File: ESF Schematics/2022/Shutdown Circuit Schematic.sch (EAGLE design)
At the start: 59 parts, among them K1 RELAY_DPDT_RT424009, K2 RELAY_SPST_NO_

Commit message: final drafts of most schematics
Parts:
- removed U$16: CONNECTOR-2_HPK, HyTechSymbolsTemp:CONNECTOR-2_HPK
- added J1, J2: CONNECTOR-1_LCAX2-14F-E, HyTechSymbolsTemp:CONNECTOR-1_LCAX2-14F-E
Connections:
- net TS+UNFUSED: now also J2.1; no longer U$16.1
- net TS-UNFUSED: now also J1.1; no longer U$16.2
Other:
- note added: "16AWG"
- note added: "16AWG:"
- note added: "17.5mm^2"
- note added: "17.5mm^2:"
- note added: "22AWG"
- note added: "22AWG:"
- note added: "Wire Gauge Key"
- moved on the sheet: F6

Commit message: ESF review changes
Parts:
- renumbered K1 to BSPD_RELAY
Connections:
- new net N$42: BSPD_RELAY.5, SOFTWARE_SHDN_RELAY.6
- net N$10: now also BSPD_RELAY.6
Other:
- note added: "HVD connectors Move interlocks outside put actual battery symbol Fix power switching circuit relay and add to datasheet Make TSMS after interlocks also reference accumulator notes ring terminals"
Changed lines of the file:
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@@
 <part name="P3" library="HyTechSupplies" deviceset="GND" device=""/>
 <part name="LATCHING" library="HyTechSymbolsTemp" deviceset="BUTTON_NO" device=""/>
-<part name="K1" library="HyTechSymbolsTemp" deviceset="RELAY_DPDT_?*" device="" technology="RT424009"/>
+<part name="BSPD_RELAY" library="HyTechSymbolsTemp" deviceset="RELAY_DPDT_?*" device="" technology="RT424009"/>
 <part name="U$7" library="HyTechSymbolsTemp" deviceset="DIODE" device=""/>
 <part name="U$8" library="HyTechSymbolsTemp" deviceset="DIODE" device=""/>
@@
 <text x="114.3" y="63.5" size="1.27" layer="97" align="top-left">22AWG</text>
 <text x="76.2" y="162.56" size="1.27" layer="97" align="top-left">22AWG</text>
+<text x="289.56" y="203.2" size="1.778" layer="88">HVD connectors
+Move interlocks outside
+put actual battery symbol
+Fix power switching circuit relay and add to datasheet
+Make TSMS after interlocks
+also reference accumulator notes
+ring terminals
+</text>
 </plain>
 <instances>
@@
 <attribute name="NAME" x="157.48" y="203.962" size="1.27" layer="95" align="bottom-center"/>
 </instance>
-<instance part="K1" gate="G$1" x="203.2" y="175.26" smashed="yes">
+<instance part="BSPD_RELAY" gate="G$1" x="203.2" y="175.26" smashed="yes">
 <attribute name="MPN" x="203.2" y="141.478" size="1.27" layer="96" align="top-left"/>
 <attribute name="NAME" x="203.2" y="176.022" size="1.27" layer="95"/>
@@
 <pinref part="AMS_RELAY" gate="G$1" pin="5"/>
 <wire x1="175.26" y1="149.86" x2="175.26" y2="147.32" width="0.1524" layer="91"/>
+<pinref part="BSPD_RELAY" gate="G$1" pin="6"/>
+<wire x1="175.26" y1="147.32" x2="200.66" y2="147.32" width="0.1524" layer="91"/>
 </segment>
 </net>
@@
 <pinref part="U$7" gate="G$1" pin="A"/>
 <wire x1="200.66" y1="167.64" x2="198.12" y2="167.64" width="0.1524" layer="91"/>
-<pinref part="K1" gate="G$1" pin="COIL-"/>
-<pinref part="K1" gate="G$1" pin="3"/>
+<pinref part="BSPD_RELAY" gate="G$1" pin="COIL-"/>
+<pinref part="BSPD_RELAY" gate="G$1" pin="3"/>
 <wire x1="200.66" y1="167.64" x2="200.66" y2="157.48" width="0.1524" layer="91"/>
 <junction x="200.66" y="167.64"/>
@@
 <pinref part="U$8" gate="G$1" pin="C"/>
 <wire x1="210.82" y1="182.88" x2="215.9" y2="182.88" width="0.1524" layer="91"/>
-<pinref part="K1" gate="G$1" pin="COIL+"/>
+<pinref part="BSPD_RELAY" gate="G$1" pin="COIL+"/>
 <wire x1="215.9" y1="167.64" x2="218.44" y2="167.64" width="0.1524" layer="91"/>
 <junction x="215.9" y="167.64"/>
@@
 </segment>
 </net>
+<net name="N$42" class="0">
+<segment>
+<pinref part="BSPD_RELAY" gate="G$1" pin="5"/>
+<wire x1="215.9" y1="149.86" x2="215.9" y2="147.32" width="0.1524" layer="91"/>
+<pinref part="SOFTWARE_SHDN_RELAY" gate="G$1" pin="6"/>
+<wire x1="215.9" y1="147.32" x2="241.3" y2="147.32" width="0.1524" layer="91"/>
+</segment>
+</net>

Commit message: fixups after the ESF review
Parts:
- removed K2: RELAY_SPST_NO_, HyTechSymbolsTemp:RELAY_SPST_NO_
- added GLV_BATTERY: BATTERY, HyTechSymbols:BATTERY
- added J3, J4: CONNECTOR-1_LCAX2-14F-E, HyTechSymbolsTemp:CONNECTOR-1_LCAX2-14F-E
- added K1: RELAY_SPST_NO_CMX60D20, HyTechSymbolsTemp:RELAY_SPST_NO_CMX60D20
- added U$20, U$34, U$35, U$36, U$37: MAINTENANCE_PLUG_104742-2, HyTechSymbolsTemp:MAINTENANCE_PLUG_104742-2
- added U$38, U$39, U$40: RING_TERMINAL_19054-0042, HyTechSymbolsTemp:RING_TERMINAL_19054-0042
- U$21, U$22, U$23, U$24, U$25: value CONNECTOR-2_104742-2 -> MAINTENANCE_PLUG_104742-2; device HyTechSymbolsTemp:CONNECTOR-2_104742-2 -> HyTechSymbolsTemp:MAINTENANCE_PLUG_104742-2
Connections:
- removed net VBAT: F1.1
- new net N$43: U$20.P$1, U$21.P$1
- new net N$44: U$22.P$1, U$23.P$1
- new net N$45: U$24.P$1, U$25.P$1
- new net N$46: U$36.P$1, U$37.P$1
- new net N$47: AIR-.CONTACT1, U$37.1
- new net N$48: F6.2, U$38.P$1
- new net N$50: F5.2, U$39.P$1
- new net N$51: HPK_INTERLOCK.S, TSMS.P
- net GND: now also GLV_BATTERY.P$2, K1.COIL+; no longer K2.COIL+
- net N$13: now also HVD_INTERLOCK.P; no longer TSMS.P
- net N$14: now also F1.1, GLV_BATTERY.P$1; no longer HVD_INTERLOCK.P, TSMS.S
- net N$15: now also K1.CONTACT1; no longer K2.CONTACT1
- net N$16: now also K1.CONTACT2; no longer K2.CONTACT2
- net N$17: now also K1.COIL-; no longer K2.COIL-
- net N$23: now also U$36.1; no longer U$24.2
- net N$31: now also U$20.1; no longer U$21.2
- net N$33: now also U$22.1; no longer U$22.2
- net N$34: now also U$23.1; no longer U$22.1
- net N$35: now also U$24.1; no longer U$23.2
- net N$36: now also U$25.1; no longer U$23.1
- net N$37: now also U$34.P$1, U$35.P$1; no longer AIR-.CONTACT1, U$24.1
- net N$38: now also U$34.1, U$40.P$1; no longer U$25.2
- net PACK+: now also U$35.1, U$40.P$2; no longer U$25.1
- net RELAY_CTRL: now also U$17.PRECHARGE_OK; no longer U$17.RELAY_CTRL
- net SHDN: now also TSMS.S, U$17.VCC; no longer HPK_INTERLOCK.S, U$17.12V
- net TS+UNFUSED: now also U$39.P$2; no longer F5.2
- net TS-UNFUSED: now also J3.1, J4.1, U$38.P$2; no longer F6.2
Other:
- note added: "(>= 6 mil)"
- note added: "(Busbar)"
- note added: "HVD connectors-done Move interlocks outside-done put actual battery symbol-done Fix power switching circuit relay and add to datasheet-done Make TSMS after interlocks-done also reference accumulator notes-done ring terminals-done"
- note added: "PCB Trace"
- note added: "PCB Trace:"
- note removed: "HVD connectors Move interlocks outside put actual battery symbol Fix power switching circuit relay and add to datasheet Make TSMS after interlocks also reference accumulator notes ring terminals"
- moved on the sheet: AIR+, AIR-, F4, F5, F6, HPK_INTERLOCK, HVD_INTERLOCK, MAIN_FUSE, TSMS

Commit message: yet more fixes in preparation for submission
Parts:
- removed U$18: LOGICGATE_INVERTER, HyTechSymbolsTemp:LOGICGATE_INVERTER
- removed U$19: MOSFET_N-CHANNEL, HyTechSymbolsTemp:MOSFET_N-CHANNEL
- DISCHARGE_RES: value 10K -> 10k
- F3: value FUSE -> 3A
- PRECHARGE_RES: value 1.5K -> 7.5k
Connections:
- removed net N$24: U$18.!IN, U$19.G
- removed net N$25: PRECHARGE.COIL+, U$19.D
- removed net OKHS: U$10.OKHS
- new net +12V: U$10.+12V
- net GND: no longer U$19.S
- net IMD_OK: now also U$10.OKHS
- net PRECHARGE_OK: now also PRECHARGE.COIL+; no longer U$18.IN
- net SHDN: no longer U$10.+12V
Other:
- note removed: "HVD connectors-done Move interlocks outside-done put actual battery symbol-done Fix power switching circuit relay and add to datasheet-done Make TSMS after interlocks-done also reference accumulator notes-done ring terminals-done"
- moved on the sheet: F4

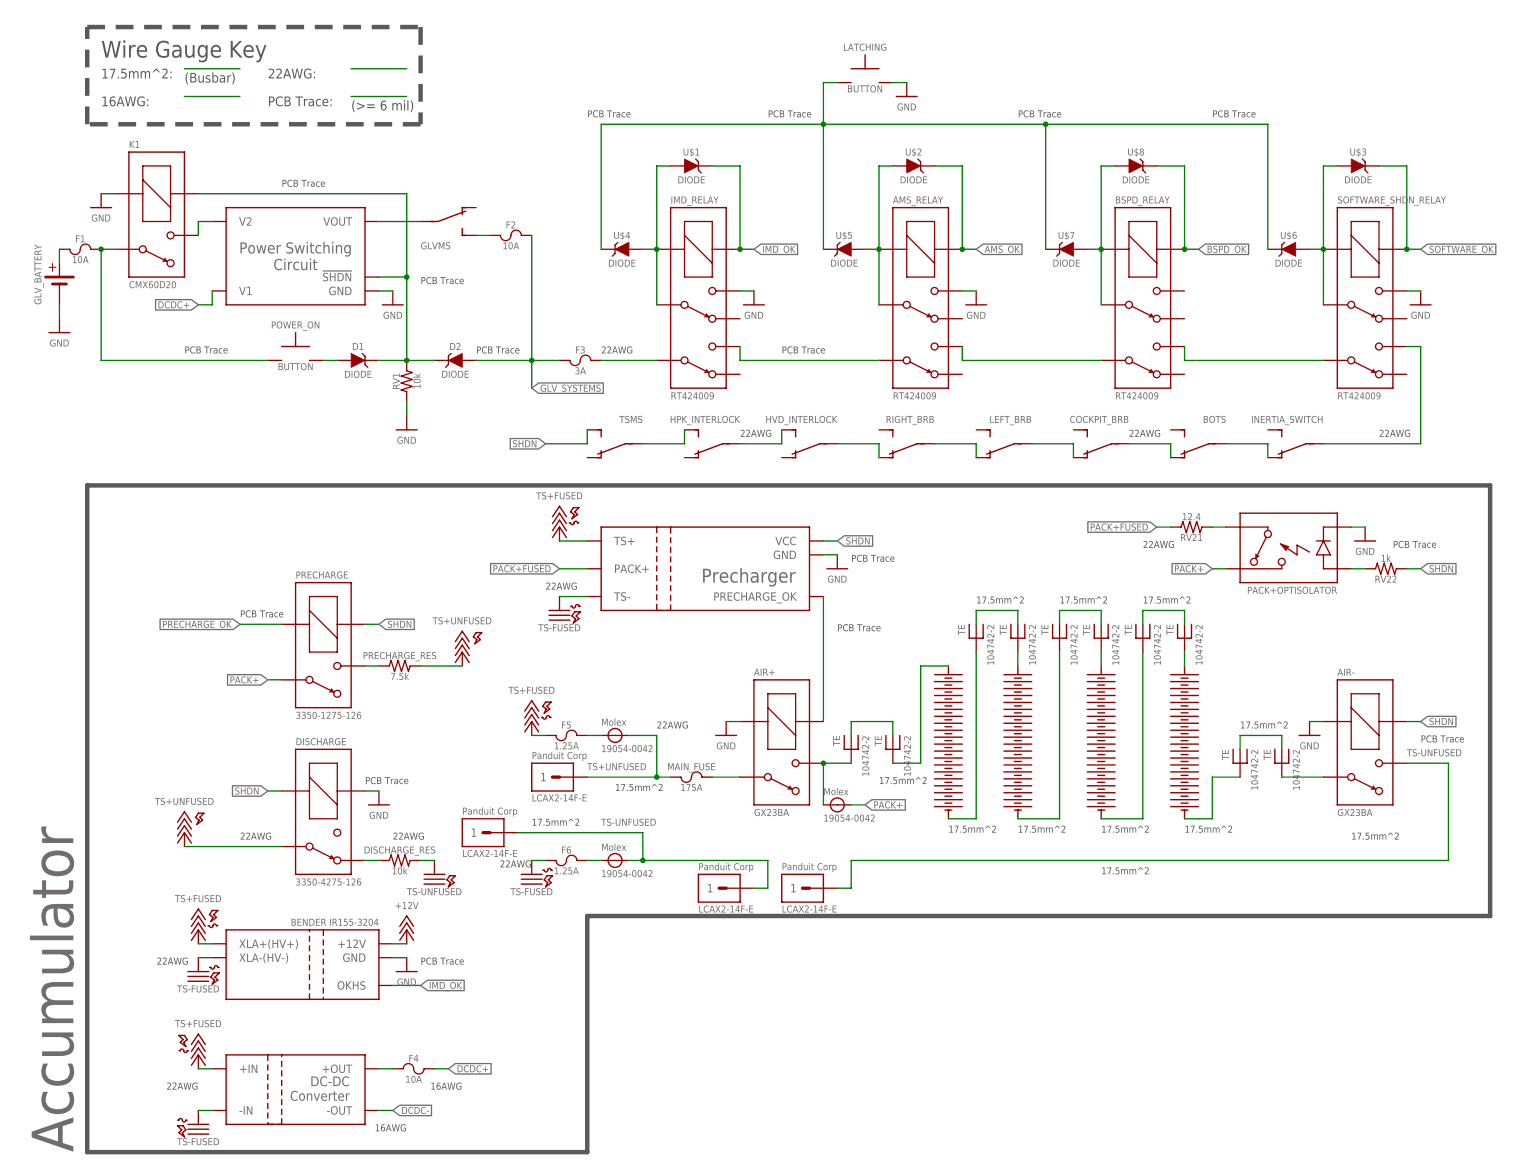
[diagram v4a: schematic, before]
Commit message: all but TSAL updated
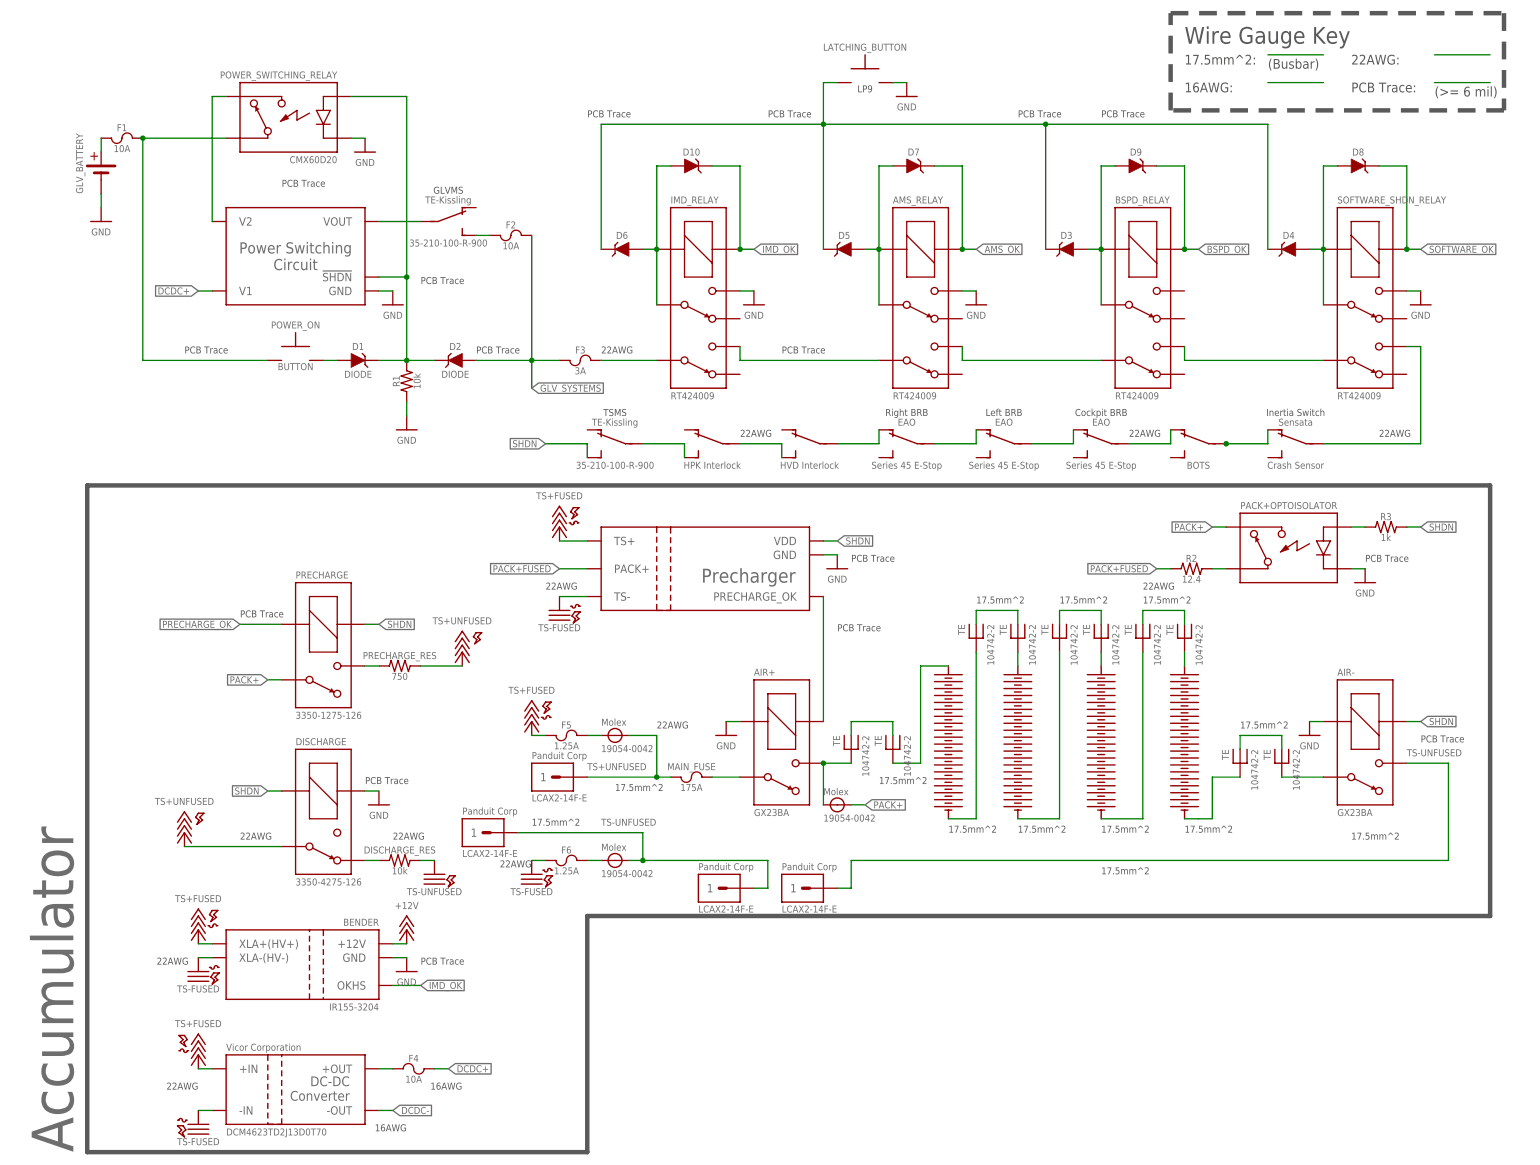
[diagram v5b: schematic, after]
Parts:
- removed BOTS, COCKPIT_BRB, GLVMS, HPK_INTERLOCK, HVD_INTERLOCK, INERTIA_SWITCH, LEFT_BRB, RIGHT_BRB, TSMS: SWITCH_SPST, HyTechSymbols:SWITCH_SPST
- removed K1: RELAY_SPST_NO_CMX60D20, HyTechSymbolsTemp:RELAY_SPST_NO_CMX60D20
- removed LATCHING: BUTTON_NO, HyTechSymbolsTemp:BUTTON_NO
- removed PACK+OPTISOLATOR: RELAY_SOLIDSTATE_NO, HyTechSymbolsTemp:RELAY_SOLIDSTATE_NO
- removed RV1: 10k, HyTechDevices:RESISTOR_VALUE
- removed RV21: 12.4, HyTechDevices:RESISTOR_VALUE
- removed RV22: 1k, HyTechDevices:RESISTOR_VALUE
- removed U$11: DC-DC_CONVERTER, HyTechSymbols:DC-DC_CONVERTER
- added D10: DIODE, HyTechSymbolsTemp:DIODE
- added LATCHING_BUTTON: BUTTON_NO_LP9, HyTechSymbolsTemp:BUTTON_NO_LP9
- added PACK+OPTOISOLATOR: RELAY_SOLIDSTATE_NO_, HyTechSymbolsTemp:RELAY_SOLIDSTATE_NO_
- added POWER_SWITCHING_RELAY: RELAY_SOLIDSTATE_NO_CMX60D20, HyTechSymbolsTemp:RELAY_SOLIDSTATE_NO_CMX60D20
- added R1: 10k, HyTechSymbolsTemp:RESISTOR
- added R2: 12.4, HyTechSymbolsTemp:RESISTOR
- added R3: 1k, HyTechSymbolsTemp:RESISTOR
- added S1: SWITCH_SPST_INERTIA_SWITCH, HyTechSymbols:SWITCH_SPST_INERTIA_SWITCH
- added S2, S6, S7: SWITCH_SPST_, HyTechSymbols:SWITCH_SPST_
- added S3: SWITCH_SPST_34MM_STOP, HyTechSymbols:SWITCH_SPST_34MM_STOP
- added S4, S5: SWITCH_SPST_40MM_STOP, HyTechSymbols:SWITCH_SPST_40MM_STOP
- added S8, S9: SWITCH_SPST_35-210-100-R-900, HyTechSymbols:SWITCH_SPST_35-210-100-R-900
- DISCHARGE_RES: device HyTechDevices:RESISTOR_VALUE -> HyTechSymbolsTemp:RESISTOR
- PRECHARGE_RES: value 7.5k -> 750; device HyTechDevices:RESISTOR_VALUE -> HyTechSymbolsTemp:RESISTOR
- U$1: value DIODE -> DC-DC_CONVERTER_DCM4623TD2J13D0T70; device HyTechSymbolsTemp:DIODE -> HyTechSymbols:DC-DC_CONVERTER_DCM4623TD2J13D0T70
- renumbered U$2 to D7, U$3 to D8, U$4 to D6, U$5 to D5, U$6 to D4, U$7 to D3, U$8 to D9
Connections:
- net DCDC-: now also U$1.-OUT; no longer U$11.-OUT
- net GND: now also LATCHING_BUTTON.P$2, PACK+OPTOISOLATOR.CONTROL-, POWER_SWITCHING_RELAY.CONTROL-, R1.1; no longer K1.COIL+, LATCHING.P$2, PACK+OPTISOLATOR.CONTROL-, RV1.1
- net IMD_OK: now also D10.C; no longer U$1.C
- net N$1: now also D10.A; no longer U$1.A
- net N$12: now also S4.O, S5.P; no longer LEFT_BRB.O, RIGHT_BRB.P
- net N$13: now also S5.O, S6.P; no longer HVD_INTERLOCK.P, RIGHT_BRB.O
- net N$15: now also POWER_SWITCHING_RELAY.CONTACT1; no longer K1.CONTACT1
- net N$16: now also POWER_SWITCHING_RELAY.CONTACT2; no longer K1.CONTACT2
- net N$17: now also POWER_SWITCHING_RELAY.CONTROL+, R1.2; no longer K1.COIL-, RV1.2
- net N$18: now also S9.P; no longer GLVMS.P
- net N$2: now also LATCHING_BUTTON.P$1; no longer LATCHING.P$1
- net N$20: now also S9.S; no longer GLVMS.S
- net N$21: now also S6.S, S7.P; no longer HPK_INTERLOCK.P, HVD_INTERLOCK.S
- net N$30: now also U$1.+OUT; no longer U$11.+OUT
- net N$39: now also PACK+OPTOISOLATOR.CONTROL+, R3.1; no longer PACK+OPTISOLATOR.CONTROL+, RV22.2
- net N$4: now also S1.O, S2.P; no longer BOTS.P, INERTIA_SWITCH.O
- net N$40: now also PACK+OPTOISOLATOR.CONTACT1, R2.2; no longer PACK+OPTISOLATOR.CONTACT1, RV21.1
- net N$51: now also S7.S, S8.P; no longer HPK_INTERLOCK.S, TSMS.P
- net N$7: now also S1.P; no longer INERTIA_SWITCH.P
- net N$8: now also S3.O, S4.P; no longer COCKPIT_BRB.O, LEFT_BRB.P
- net N$9: now also S2.O, S3.P; no longer BOTS.O, COCKPIT_BRB.P
- net PACK+: now also PACK+OPTOISOLATOR.CONTACT2; no longer PACK+OPTISOLATOR.CONTACT2
- net PACK+FUSED: now also R2.1; no longer RV21.2
- net SHDN: now also R3.2, S8.S, U$17.VDD; no longer RV22.1, TSMS.S, U$17.VCC
- net TS+: now also U$1.+IN; no longer U$11.+IN
- net TS-UNFUSED: now also U$1.-IN; no longer U$11.-IN
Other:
- note added: "Cockpit BRB"
- note added: "GLVMS"
- note added: "Inertia Switch"
- note added: "Left BRB"
- note added: "Right BRB"
- note added: "TSMS"
- moved on the sheet: F1, GLV_BATTERY
